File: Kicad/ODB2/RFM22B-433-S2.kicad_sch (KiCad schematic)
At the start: 0 parts

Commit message: edit titles
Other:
- company: (none) -> GAUL
- title: (none) -> Beacon
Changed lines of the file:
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@@
 	(generator_version "8.0")
 	(paper "A4")
+	(title_block
+		(title "Beacon")
+		(date "2024-11-09")
+		(company "GAUL")
+	)
 )

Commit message: add titles
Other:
- note added: "Beacon"
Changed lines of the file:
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@@
 		(company "GAUL")
 	)
+	(text "Beacon"
+		(exclude_from_sim no)
+		(at 31.75 18.796 0)
+		(effects
+			(font
+				(size 6 6)
+				(thickness 1.2)
+				(bold yes)
+			)
+		)
+	)
 )

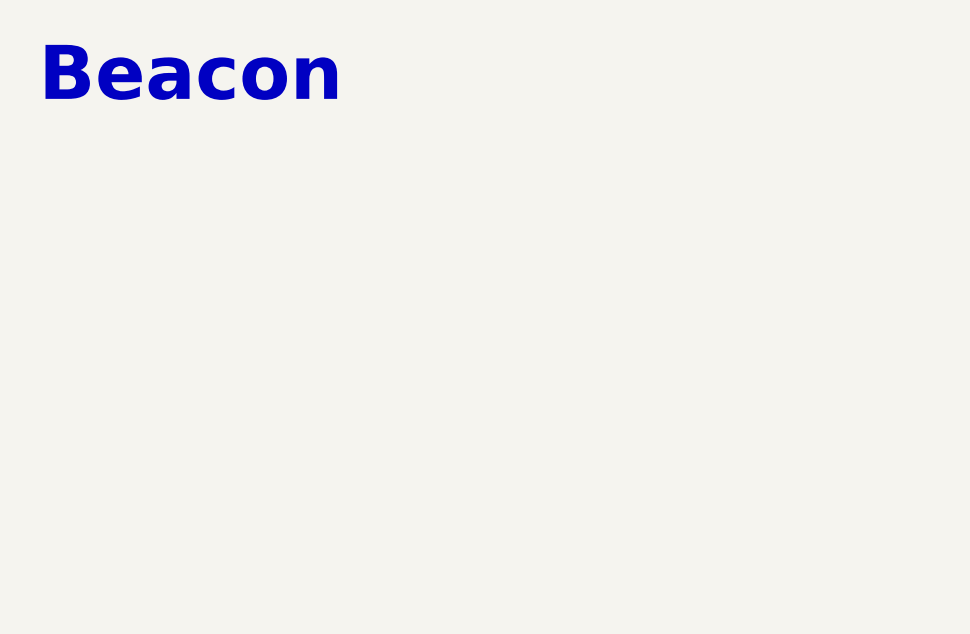
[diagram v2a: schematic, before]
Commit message: fix pinout
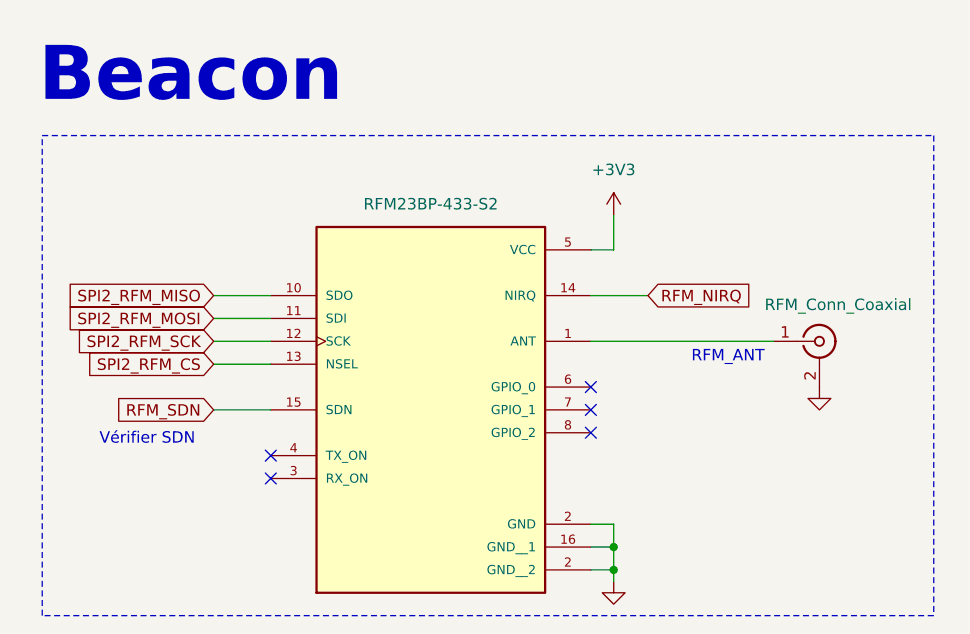
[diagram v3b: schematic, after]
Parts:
- added J6: RFM_Conn_Coaxial, symbol Connector:Conn_Coaxial
- added U9: RFM23BP-433-S2, RFM23BP-433-S2:MODULE_RFM23BP-433-S2, symbol ODB2:RFM23BP-433-S2
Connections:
- new net: J6.1 (In), U9.1 (ANT)
- new net +3V3: U9.5 (VCC)
- new net GND: J6.2 (Ext), U9.16 (GND__1), U9.2 (GND__2)
- new net RFM_NIRQ: U9.14 (NIRQ)
- new net RFM_SDN: U9.15 (SDN)
- new net SPI2_RFM_CS: U9.13 (NSEL)
- new net SPI2_RFM_MISO: U9.10 (SDO)
- new net SPI2_RFM_MOSI: U9.11 (SDI)
- new net SPI2_RFM_SCK: U9.12 (SCK)
- no-connect marks 0 -> 5
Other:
- note added: "RFM_ANT"
- note added: "Vérifier SDN"

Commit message: Revert "fix pinout"
This reverts commit f7fb1bb1343b18ec7defcf1dc44a3e70818eed55.
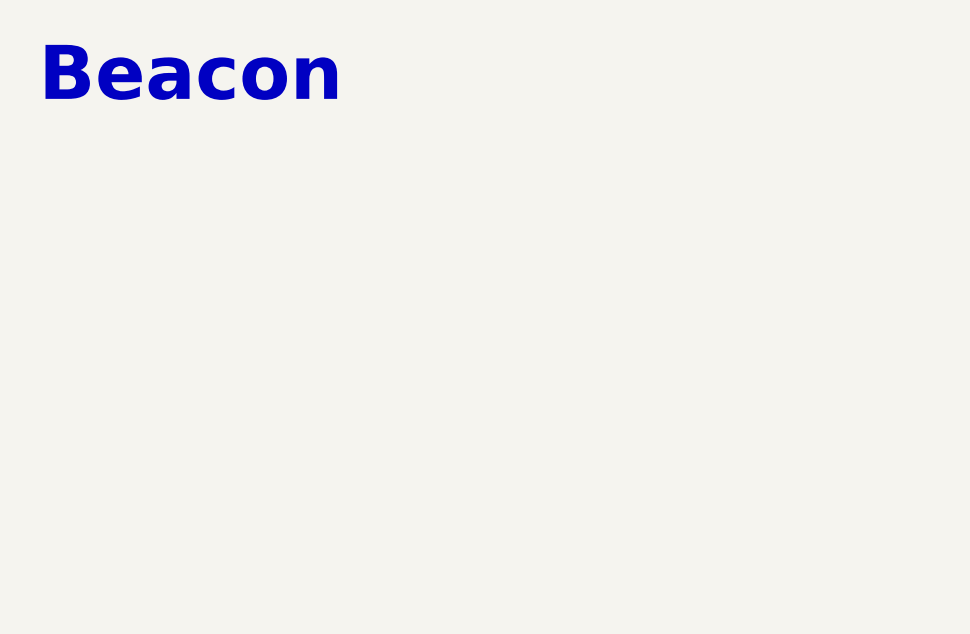
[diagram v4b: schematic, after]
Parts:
- removed J6: RFM_Conn_Coaxial, symbol Connector:Conn_Coaxial
- removed U9: RFM23BP-433-S2, RFM23BP-433-S2:MODULE_RFM23BP-433-S2, symbol ODB2:RFM23BP-433-S2
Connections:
- no-connect marks 5 -> 0
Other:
- note removed: "RFM_ANT"
- note removed: "Vérifier SDN"

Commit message: add rfm
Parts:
- added J6: RFM_Conn_Coaxial, symbol Connector:Conn_Coaxial
- added U9: RFM23BP-433-S2, RFM23BP-433-S2:MODULE_RFM23BP-433-S2, symbol ODB2:RFM23BP-433-S2
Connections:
- new net +3V3: U9.5 (VCC)
- new net GND: J6.2 (Ext), U9.16 (GND__1), U9.2 (GND__2)
- new net RFM_ANT: J6.1 (In), U9.1 (ANT)
- new net RFM_NIRQ: U9.14 (NIRQ)
- new net RFM_SDN: U9.15 (SDN)
- new net SPI2_RFM_CS: U9.13 (NSEL)
- new net SPI2_RFM_MISO: U9.10 (SDO)
- new net SPI2_RFM_MOSI: U9.11 (SDI)
- new net SPI2_RFM_SCK: U9.12 (SCK)
- no-connect marks 0 -> 5

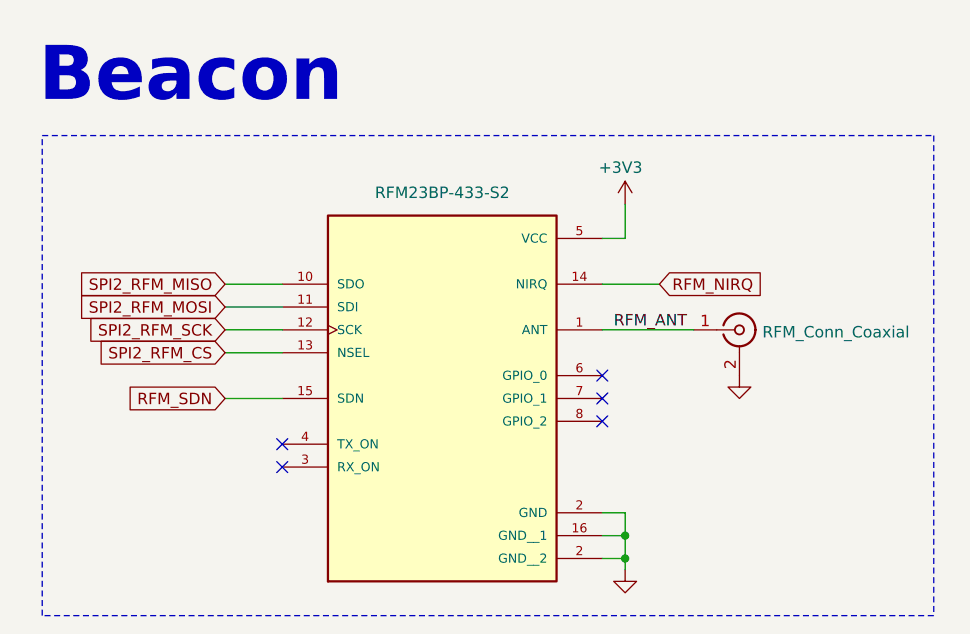
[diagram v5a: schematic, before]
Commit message: merge all sensors to main page + fix NC
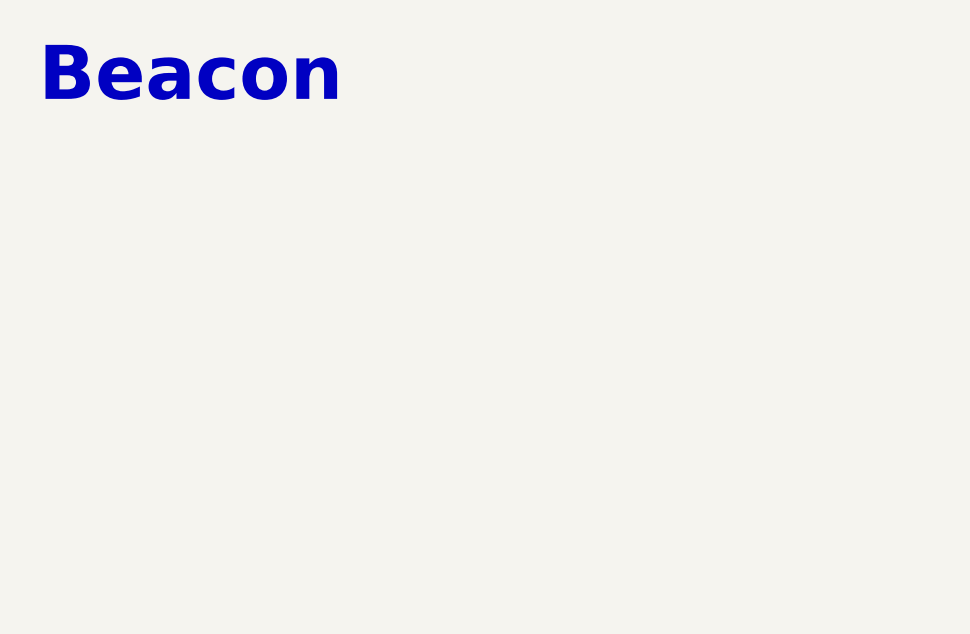
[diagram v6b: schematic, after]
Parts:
- removed J6: RFM_Conn_Coaxial, symbol Connector:Conn_Coaxial
- removed U9: RFM23BP-433-S2, RFM23BP-433-S2:MODULE_RFM23BP-433-S2, symbol ODB2:RFM23BP-433-S2
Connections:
- no-connect marks 5 -> 0
